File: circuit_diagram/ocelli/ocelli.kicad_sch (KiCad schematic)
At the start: 114 parts, among them J1 Conn_01x06, J2 Conn_01x06, J3 Conn_01x06, J4 Conn_01x06, J5 Conn_01x08, J6 Conn_01x02, J7 Conn_01x02, Q1 BSS138, Q10 BSS138, Q2 ST-1KL3A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

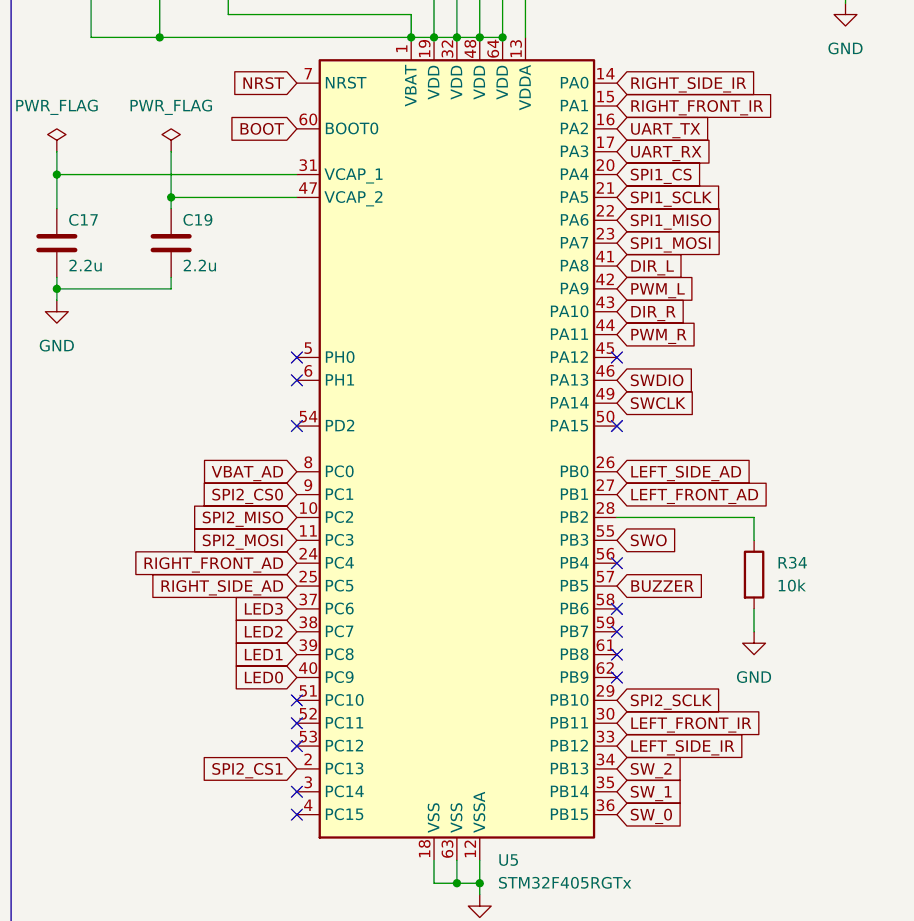
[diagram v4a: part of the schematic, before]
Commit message: 対処すべきDRCエラーに対処した
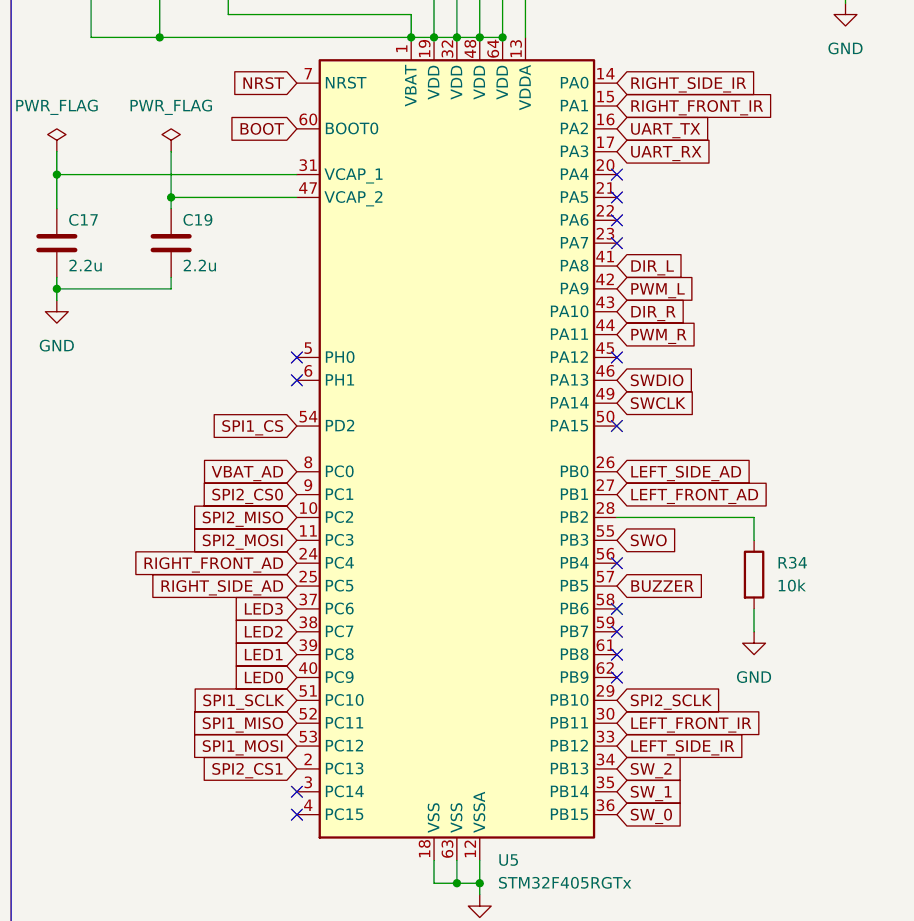
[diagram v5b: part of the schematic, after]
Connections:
- net SPI1_CS: now also U5.54 (PD2); no longer U5.20 (PA4)
- net SPI1_MISO: now also U5.52 (PC11); no longer U5.22 (PA6)
- net SPI1_MOSI: now also U5.53 (PC12); no longer U5.23 (PA7)
- net SPI1_SCLK: now also U5.51 (PC10); no longer U5.21 (PA5)
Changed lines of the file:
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@@
   (no_connect (at 102.87 271.78))
   (no_connect (at 233.68 162.56))
-  (no_connect (at 233.68 170.18))
+  (no_connect (at 269.24 142.24))
   (no_connect (at 233.68 165.1))
   (no_connect (at 233.68 210.82))
   (no_connect (at 233.68 213.36))
-  (no_connect (at 233.68 200.66))
-  (no_connect (at 233.68 205.74))
-  (no_connect (at 233.68 203.2))
   (no_connect (at 269.24 185.42))
   (no_connect (at 269.24 190.5))
@@
   (no_connect (at 35.56 49.53))
   (no_connect (at 269.24 162.56))
+  (no_connect (at 269.24 144.78))
+  (no_connect (at 269.24 147.32))
+  (no_connect (at 269.24 149.86))
   (no_connect (at 173.99 243.84))
   (no_connect (at 173.99 213.36))
@@
     )
   )
-  (global_label "SPI1_MISO" (shape input) (at 269.24 147.32 0) (fields_autoplaced)
-    (effects (font (size 1.27 1.27)) (justify left))
-    (property "Intersheet References" "${INTERSHEET_REFS}" (id 0) (at 281.5107 147.3994 0)
-      (effects (font (size 1.27 1.27)) (justify left) hide)
+  (global_label "SPI1_MISO" (shape input) (at 233.68 203.2 180) (fields_autoplaced)
+    (effects (font (size 1.27 1.27)) (justify right))
+    (property "Intersheet References" "${INTERSHEET_REFS}" (id 0) (at 221.4093 203.1206 0)
+      (effects (font (size 1.27 1.27)) (justify right) hide)
     )
   )
@@
     )
   )
-  (global_label "SPI1_MOSI" (shape input) (at 269.24 149.86 0) (fields_autoplaced)
-    (effects (font (size 1.27 1.27)) (justify left))
-    (property "Intersheet References" "${INTERSHEET_REFS}" (id 0) (at 281.5107 149.7806 0)
-      (effects (font (size 1.27 1.27)) (justify left) hide)
+  (global_label "SPI1_MOSI" (shape input) (at 233.68 205.74 180) (fields_autoplaced)
+    (effects (font (size 1.27 1.27)) (justify right))
+    (property "Intersheet References" "${INTERSHEET_REFS}" (id 0) (at 221.4093 205.8194 0)
+      (effects (font (size 1.27 1.27)) (justify right) hide)
     )
   )
@@
     )
   )
-  (global_label "SPI1_CS" (shape input) (at 269.24 142.24 0) (fields_autoplaced)
-    (effects (font (size 1.27 1.27)) (justify left))
-    (property "Intersheet References" "${INTERSHEET_REFS}" (id 0) (at 279.3941 142.1606 0)
-      (effects (font (size 1.27 1.27)) (justify left) hide)
+  (global_label "SPI1_CS" (shape input) (at 233.68 170.18 180) (fields_autoplaced)
+    (effects (font (size 1.27 1.27)) (justify right))
+    (property "Intersheet References" "${INTERSHEET_REFS}" (id 0) (at 223.5259 170.2594 0)
+      (effects (font (size 1.27 1.27)) (justify right) hide)
     )
   )
@@
     )
   )
-  (global_label "SPI1_SCLK" (shape input) (at 269.24 144.78 0) (fields_autoplaced)
-    (effects (font (size 1.27 1.27)) (justify left))
-    (property "Intersheet References" "${INTERSHEET_REFS}" (id 0) (at 281.6921 144.7006 0)
-      (effects (font (size 1.27 1.27)) (justify left) hide)
-    )
-  )
+  (global_label "SPI1_SCLK" (shape input) (at 233.68 200.66 180) (fields_autoplaced)
+    (effects (font (size 1.27 1.27)) (justify right))
+    (property "Intersheet References" "${INTERSHEET_REFS}" (id 0) (at 221.2279 200.7394 0)
+      (effects (font (size 1.27 1.27)) (justify right) hide)
+    )
+  )

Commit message: フットプリント修正
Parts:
- U4: footprint Package_DFN_QFN:HVQFN-24-1EP_4x4mm_P0.5mm_EP2.1x2.1mm -> Package_DFN_QFN:QFN-24-1EP_3x3mm_P0.4mm_EP1.75x1.6mm
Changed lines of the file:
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@@
     (property "Reference" "U4" (id 0) (at 186.69 215.6712 0))
     (property "Value" "ICM-20649" (id 1) (at 186.69 218.2112 0))
-    (property "Footprint" "Package_DFN_QFN:HVQFN-24-1EP_4x4mm_P0.5mm_EP2.1x2.1mm" (id 2) (at 167.64 228.6 0)
+    (property "Footprint" "Package_DFN_QFN:QFN-24-1EP_3x3mm_P0.4mm_EP1.75x1.6mm" (id 2) (at 167.64 228.6 0)
       (effects (font (size 1.27 1.27)) hide)
     )
@@
     )
     (path "/071c0607-01c4-409b-a94e-86fba83646e8"
-      (reference "U4") (unit 1) (value "ICM-20649") (footprint "Package_DFN_QFN:HVQFN-24-1EP_4x4mm_P0.5mm_EP2.1x2.1mm")
+      (reference "U4") (unit 1) (value "ICM-20649") (footprint "Package_DFN_QFN:QFN-24-1EP_3x3mm_P0.4mm_EP1.75x1.6mm")
     )
     (path "/6262fdac-0b24-4b37-921e-3759af0201d4"

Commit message: 部品リスト追加
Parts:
- J5: url (none) -> https://akizukidenshi.com/catalog/g/gC-03866/
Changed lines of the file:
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@@
+      (effects (font (size 1.27 1.27)) hide)
+    )
+    (property "url" "https://akizukidenshi.com/catalog/g/gC-03866/" (id 4) (at 223.52 49.53 0)
       (effects (font (size 1.27 1.27)) hide)
     )
